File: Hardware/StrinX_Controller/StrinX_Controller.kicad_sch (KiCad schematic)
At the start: 0 parts

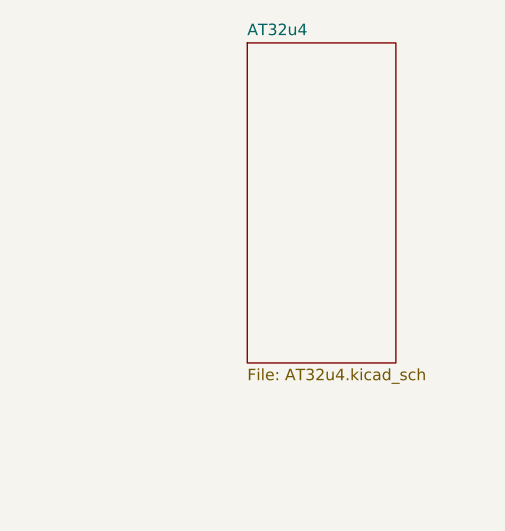
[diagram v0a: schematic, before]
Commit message: Add new input pins to StrinX_Controller schematic
Expanded the StrinX_Controller.kicad_sch sheet size and added multiple new input pins for various signals (JoyXA, JoyYA, JoyXB, JoyYB, SW1-SW4, BTN, CK, DT, SCL, SDA, SPI, USB, etc.). Also updated AT32u4.kicad_sch to fix a power reference and add a new power path instance.
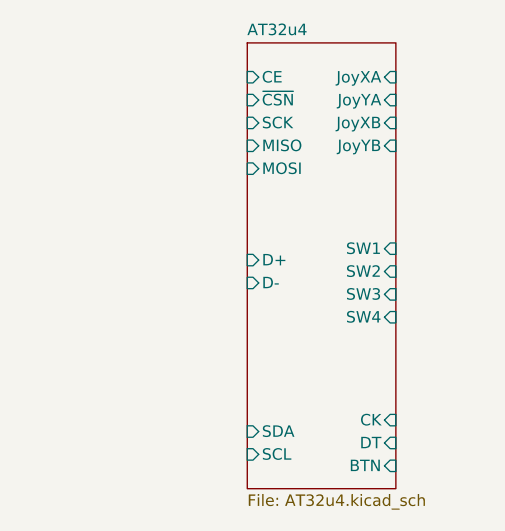
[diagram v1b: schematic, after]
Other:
- sheet AT32u4 ports: added BTN, CE, CK, D+, D-, DT, JoyXA, JoyXB, JoyYA, JoyYB, MISO, MOSI, SCK, SCL, SDA, SW1, SW2, SW3, SW4, ~{CSN}; removed none
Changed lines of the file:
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@@
 	(sheet
 		(at 114.3 63.5)
-		(size 16.51 35.56)
+		(size 16.51 49.53)
 		(exclude_from_sim no)
 		(in_bom yes)
@@
 		)
 		(property "Sheetfile" "AT32u4.kicad_sch"
-			(at 114.3 99.6446 0)
+			(at 114.3 113.6146 0)
 			(effects
 				(font
@@
 			)
 		)
+		(pin "SCL" input
+			(at 114.3 109.22 180)
+			(effects
+				(font
+					(size 1.27 1.27)
+				)
+				(justify left)
+			)
+		)
+		(pin "JoyXB" input
+			(at 130.81 72.39 0)
+			(effects
+				(font
+					(size 1.27 1.27)
+				)
+				(justify right)
+			)
+		)
+		(pin "CK" input
+			(at 130.81 105.41 0)
+			(effects
+				(font
+					(size 1.27 1.27)
+				)
+				(justify right)
+			)
+		)
+		(pin "SW4" input
+			(at 130.81 93.98 0)
+			(effects
+				(font
+					(size 1.27 1.27)
+				)
+				(justify right)
+			)
+		)
+		(pin "JoyYA" input
+			(at 130.81 69.85 0)
+			(effects
+				(font
+					(size 1.27 1.27)
+				)
+				(justify right)
+			)
+		)
+		(pin "SW2" input
+			(at 130.81 88.9 0)
+			(effects
+				(font
+					(size 1.27 1.27)
+				)
+				(justify right)
+			)
+		)
+		(pin "SW3" input
+			(at 130.81 91.44 0)
+			(effects
+				(font
+					(size 1.27 1.27)
+				)
+				(justify right)
+			)
+		)
+		(pin "MISO" input
+			(at 114.3 74.93 180)
+			(effects
+				(font
+					(size 1.27 1.27)
+				)
+				(justify left)
+			)
+		)
+		(pin "JoyXA" input
+			(at 130.81 67.31 0)
+			(effects
+				(font
+					(size 1.27 1.27)
+				)
+				(justify right)
+			)
+		)
+		(pin "D+" input
+			(at 114.3 87.63 180)
+			(effects
+				(font
+					(size 1.27 1.27)
+				)
+				(justify left)
+			)
+		)
+		(pin "SDA" input
+			(at 114.3 106.68 180)
+			(effects
+				(font
+					(size 1.27 1.27)
+				)
+				(justify left)
+			)
+		)
+		(pin "CE" input
+			(at 114.3 67.31 180)
+			(effects
+				(font
+					(size 1.27 1.27)
+				)
+				(justify left)
+			)
+		)
+		(pin "D-" input
+			(at 114.3 90.17 180)
+			(effects
+				(font
+					(size 1.27 1.27)
+				)
+				(justify left)
+			)
+		)
+		(pin "JoyYB" input
+			(at 130.81 74.93 0)
+			(effects
+				(font
+					(size 1.27 1.27)
+				)
+				(justify right)
+			)
+		)
+		(pin "SCK" input
+			(at 114.3 72.39 180)
+			(effects
+				(font
+					(size 1.27 1.27)
+				)
+				(justify left)
+			)
+		)
+		(pin "DT" input
+			(at 130.81 107.95 0)
+			(effects
+				(font
+					(size 1.27 1.27)
+				)
+				(justify right)
+			)
+		)
+		(pin "~{CSN}" input
+			(at 114.3 69.85 180)
+			(effects
+				(font
+					(size 1.27 1.27)
+				)
+				(justify left)
+			)
+		)
+		(pin "MOSI" input
+			(at 114.3 77.47 180)
+			(effects
+				(font
+					(size 1.27 1.27)
+				)
+				(justify left)
+			)
+		)
+		(pin "BTN" input
+			(at 130.81 110.49 0)
+			(effects
+				(font
+					(size 1.27 1.27)
+				)
+				(justify right)
+			)
+		)
+		(pin "SW1" input
+			(at 130.81 86.36 0)
+			(effects
+				(font
+					(size 1.27 1.27)
+				)
+				(justify right)
+			)
+		)

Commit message: Add NRF24L01 module
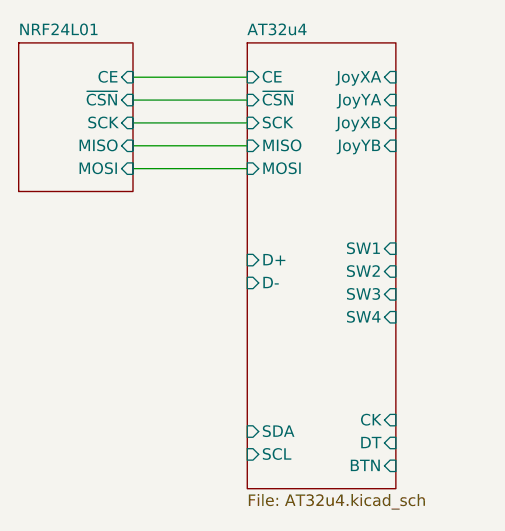
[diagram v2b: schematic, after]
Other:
- added sheet NRF24L01 (NRF24L01.kicad_sch)
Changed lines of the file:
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@@
 	(generator_version "9.0")
 	(paper "A4")
+	(wire
+		(pts
+			(xy 101.6 67.31) (xy 114.3 67.31)
+		)
+		(stroke
+			(width 0)
+			(type default)
+		)
+	)
+	(wire
+		(pts
+			(xy 101.6 69.85) (xy 114.3 69.85)
+		)
+		(stroke
+			(width 0)
+			(type default)
+		)
+	)
+	(wire
+		(pts
+			(xy 101.6 72.39) (xy 114.3 72.39)
+		)
+		(stroke
+			(width 0)
+			(type default)
+		)
+	)
+	(wire
+		(pts
+			(xy 101.6 77.47) (xy 114.3 77.47)
+		)
+		(stroke
+			(width 0)
+			(type default)
+		)
+	)
+	(wire
+		(pts
+			(xy 101.6 74.93) (xy 114.3 74.93)
+		)
+		(stroke
+			(width 0)
+			(type default)
+		)
+	)
 	(sheet
 		(at 114.3 63.5)
@@
 				)
 			)
+		)
+	)
+	(sheet
+		(at 88.9 63.5)
+		(size 12.7 16.51)
+		(exclude_from_sim no)
+		(in_bom yes)
+		(on_board yes)
+		(dnp no)
+		(fields_autoplaced yes)
+		(stroke
+			(width 0.1524)
+			(type solid)
+		)
+		(fill
+			(color 0 0 0 0.0000)
+		)
+		(property "Sheetname" "NRF24L01"
+			(at 88.9 62.7884 0)
+			(effects
+				(font
+					(size 1.27 1.27)
+				)
+				(justify left bottom)
+			)
+		)
+		(property "Sheetfile" "NRF24L01.kicad_sch"
+			(at 88.9 80.5946 0)
+			(effects
+				(font
+					(size 1.27 1.27)
+				)
+				(justify left top)
+				(hide yes)
+			)
+		)
+		(pin "MISO" input
+			(at 101.6 74.93 0)
+			(effects
+				(font
+					(size 1.27 1.27)
+				)
+				(justify right)
+			)
+		)
+		(pin "MOSI" input
+			(at 101.6 77.47 0)
+			(effects
+				(font
+					(size 1.27 1.27)
+				)
+				(justify right)
+			)
+		)
+		(pin "SCK" input
+			(at 101.6 72.39 0)
+			(effects
+				(font
+					(size 1.27 1.27)
+				)
+				(justify right)
+			)
+		)
+		(pin "~{CSN}" input
+			(at 101.6 69.85 0)
+			(effects
+				(font
+					(size 1.27 1.27)
+				)
+				(justify right)
+			)
+		)
+		(pin "CE" input
+			(at 101.6 67.31 0)
+			(effects
+				(font
+					(size 1.27 1.27)
+				)
+				(justify right)
+			)
+		)
+		(instances
+			(project "StrinX_Controller"
+				(path "/60efaa1b-44bb-4814-90d0-8b9990f45080"
+					(page "3")
+				)
+			)
